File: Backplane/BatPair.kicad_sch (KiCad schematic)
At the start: 6 parts

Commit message: All parts are correct.
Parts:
- renumbered R31 to R22, R64 to R23, R65 to R24, R89 to R25, R90 to R26, R91 to R27
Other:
- removed sheet Current Control
- added sheet Current Control1 (Current Control.kicad_sch)

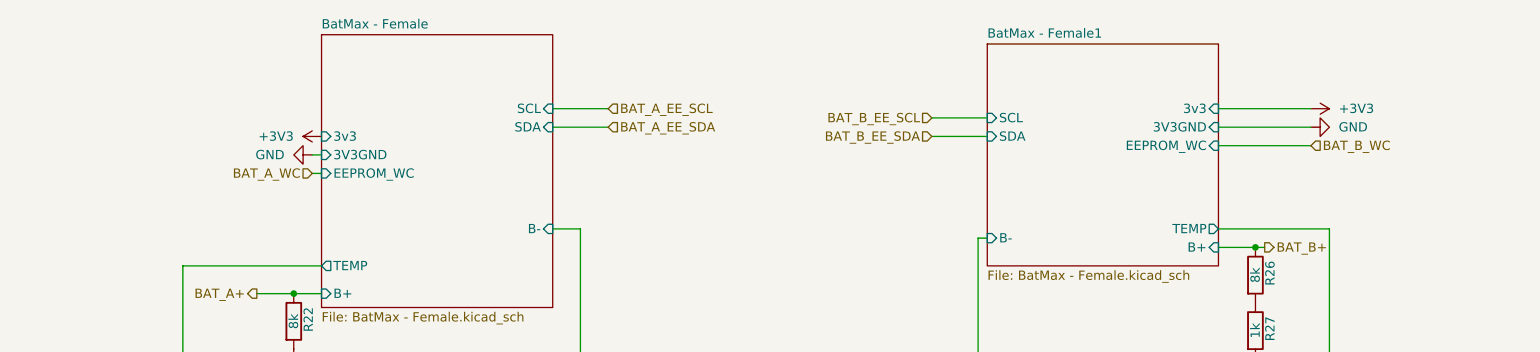
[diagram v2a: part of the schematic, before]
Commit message: First draft routing done.
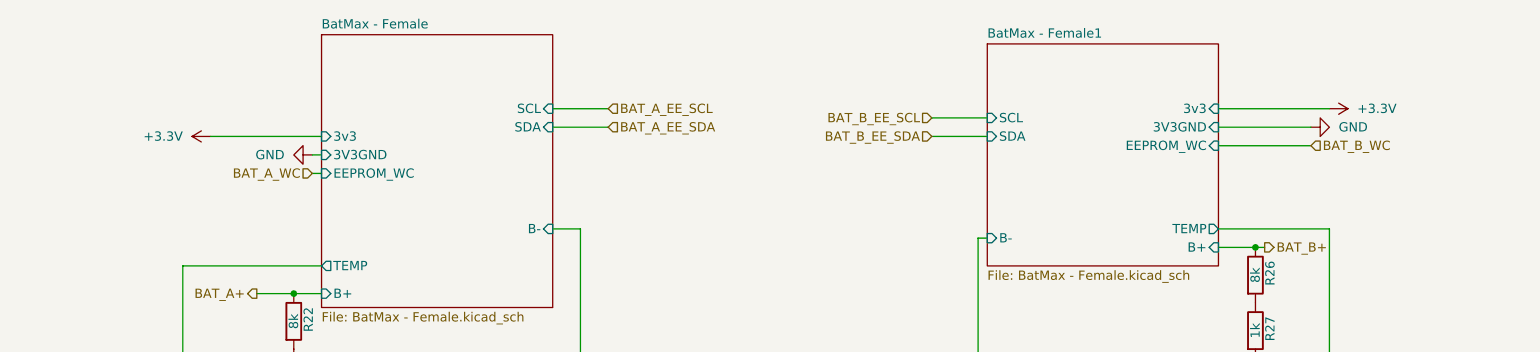
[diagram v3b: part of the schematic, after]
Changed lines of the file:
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@@
+	(wire
+		(pts
+			(xy 66.04 87.63) (xy 81.28 87.63)
+		)
+		(stroke
+			(width 0)
+			(type default)
+		)
+	)
 	(wire
 		(pts
@@
 	(wire
 		(pts
-			(xy 217.17 83.82) (xy 204.47 83.82)
-		)
-		(stroke
-			(width 0)
-			(type default)
-		)
-	)
-	(wire
-		(pts
 			(xy 237.49 129.54) (xy 237.49 130.81)
 		)
@@
 		(pts
 			(xy 73.66 140.97) (xy 59.69 140.97)
+		)
+		(stroke
+			(width 0)
+			(type default)
+		)
+	)
+	(wire
+		(pts
+			(xy 219.71 83.82) (xy 204.47 83.82)
 		)
 		(stroke
@@
 	)
 	(symbol
+		(lib_id "power:+3.3V")
+		(at 219.71 83.82 270)
+		(mirror x)
+		(unit 1)
+		(exclude_from_sim no)
+		(in_bom yes)
+		(on_board yes)
+		(dnp no)
+		(fields_autoplaced yes)
+		(property "Reference" "#PWR075"
+			(at 215.9 83.82 0)
+			(effects
+				(font
+					(size 1.27 1.27)
+				)
+				(hide yes)
+			)
+		)
+		(property "Value" "+3.3V"
+			(at 223.52 83.8199 90)
+			(effects
+				(font
+					(size 1.27 1.27)
+				)
+				(justify left)
+			)
+		)
+		(property "Footprint" ""
+			(at 219.71 83.82 0)
+			(effects
+				(font
+					(size 1.27 1.27)
+				)
+				(hide yes)
+			)
+		)
+		(property "Datasheet" ""
+			(at 219.71 83.82 0)
+			(effects
+				(font
+					(size 1.27 1.27)
+				)
+				(hide yes)
+			)
+		)
+		(property "Description" "Power symbol creates a global label with name \"+3.3V\""
+			(at 219.71 83.82 0)
+			(effects
+				(font
+					(size 1.27 1.27)
+				)
+				(hide yes)
+			)
+		)
+		(pin "1"
+		)
+		(instances
+			(project "Backplane"
+				(path "/4763d09e-4fb7-455a-b785-38411d748b6f/73c31c82-b4ce-4db9-85ed-23bc4db11f2f"
+					(reference "#PWR075")
+					(unit 1)
+				)
+				(path "/4763d09e-4fb7-455a-b785-38411d748b6f/af45f37b-7841-4d0a-9a92-a045ec353c82"
+					(reference "#PWR076")
+					(unit 1)
+				)
+			)
+		)
+	)
+	(symbol
+		(lib_id "power:+3.3V")
+		(at 66.04 87.63 90)
+		(unit 1)
+		(exclude_from_sim no)
+		(in_bom yes)
+		(on_board yes)
+		(dnp no)
+		(fields_autoplaced yes)
+		(property "Reference" "#PWR058"
+			(at 69.85 87.63 0)
+			(effects
+				(font
+					(size 1.27 1.27)
+				)
+				(hide yes)
+			)
+		)
+		(property "Value" "+3.3V"
+			(at 62.23 87.6299 90)
+			(effects
+				(font
+					(size 1.27 1.27)
+				)
+				(justify left)
+			)
+		)
+		(property "Footprint" ""
+			(at 66.04 87.63 0)
+			(effects
+				(font
+					(size 1.27 1.27)
+				)
+				(hide yes)
+			)
+		)
+		(property "Datasheet" ""
+			(at 66.04 87.63 0)
+			(effects
+				(font
+					(size 1.27 1.27)
+				)
+				(hide yes)
+			)
+		)
+		(property "Description" "Power symbol creates a global label with name \"+3.3V\""
+			(at 66.04 87.63 0)
+			(effects
+				(font
+					(size 1.27 1.27)
+				)
+				(hide yes)
+			)
+		)
+		(pin "1"
+		)
+		(instances
+			(project ""
+				(path "/4763d09e-4fb7-455a-b785-38411d748b6f/73c31c82-b4ce-4db9-85ed-23bc4db11f2f"
+					(reference "#PWR058")
+					(unit 1)
+				)
+				(path "/4763d09e-4fb7-455a-b785-38411d748b6f/af45f37b-7841-4d0a-9a92-a045ec353c82"
+					(reference "#PWR068")
+					(unit 1)
+				)
+			)
+		)
+	)
+	(symbol
 		(lib_id "power:GND")
 		(at 85.09 127 90)
@@
 					(unit 1)
 				)
-			)
-		)
-	)
-	(symbol
-		(lib_id "power:+3V3")
-		(at 217.17 83.82 270)
-		(unit 1)
-		(exclude_from_sim no)
-		(in_bom yes)
-		(on_board yes)
-		(dnp no)
-		(fields_autoplaced yes)
-		(property "Reference" "#PWR061"
-			(at 213.36 83.82 0)
-			(effects
-				(font
-					(size 1.27 1.27)
-				)
-				(hide yes)
-			)
-		)
-		(property "Value" "+3V3"
-			(at 220.98 83.8199 90)
-			(effects
-				(font
-					(size 1.27 1.27)
-				)
-				(justify left)
-			)
-		)
-		(property "Footprint" ""
-			(at 217.17 83.82 0)
-			(effects
-				(font
-					(size 1.27 1.27)
-				)
-				(hide yes)
-			)
-		)
-		(property "Datasheet" ""
-			(at 217.17 83.82 0)
-			(effects
-				(font
-					(size 1.27 1.27)
-				)
-				(hide yes)
-			)
-		)
-		(property "Description" "Power symbol creates a global label with name \"+3V3\""
-			(at 217.17 83.82 0)
-			(effects
-				(font
-					(size 1.27 1.27)
-				)
-				(hide yes)
-			)
-		)
-		(pin "1"
-		)
-		(instances
-			(project "Backplane"
-				(path "/4763d09e-4fb7-455a-b785-38411d748b6f/73c31c82-b4ce-4db9-85ed-23bc4db11f2f"
-					(reference "#PWR061")
-					(unit 1)
-				)
-				(path "/4763d09e-4fb7-455a-b785-38411d748b6f/af45f37b-7841-4d0a-9a92-a045ec353c82"
-					(reference "#PWR071")
-					(unit 1)
-				)
-			)
-		)
-	)
-	(symbol
-		(lib_id "power:+3V3")
-		(at 81.28 87.63 90)
-		(mirror x)
-		(unit 1)
-		(exclude_from_sim no)
-		(in_bom yes)
-		(on_board yes)
-		(dnp no)
-		(fields_autoplaced yes)
-		(property "Reference" "#PWR058"
-			(at 85.09 87.63 0)
-			(effects
-				(font
-					(size 1.27 1.27)
-				)
-				(hide yes)
-			)
-		)
-		(property "Value" "+3V3"
-			(at 77.47 87.6299 90)
-			(effects
-				(font
-					(size 1.27 1.27)
-				)
-				(justify left)
-			)
-		)
-		(property "Footprint" ""
-			(at 81.28 87.63 0)
-			(effects
-				(font
-					(size 1.27 1.27)
-				)
-				(hide yes)
-			)
-		)
-		(property "Datasheet" ""
-			(at 81.28 87.63 0)
-			(effects
-				(font
-					(size 1.27 1.27)
-				)
-				(hide yes)
-			)
-		)
-		(property "Description" "Power symbol creates a global label with name \"+3V3\""
-			(at 81.28 87.63 0)
-			(effects
-				(font
-					(size 1.27 1.27)
-				)
-				(hide yes)
-			)
-		)
-		(pin "1"
-		)
-		(instances
-			(project "Backplane"
-				(path "/4763d09e-4fb7-455a-b785-38411d748b6f/73c31c82-b4ce-4db9-85ed-23bc4db11f2f"
-					(reference "#PWR058")
-					(unit 1)
-				)
-				(path "/4763d09e-4fb7-455a-b785-38411d748b6f/af45f37b-7841-4d0a-9a92-a045ec353c82"
-					(reference "#PWR068")
-					(unit 1)
-				)

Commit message: added
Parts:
- removed R22, R26: 8k, Resistor_SMD:R_1206_3216Metric_Pad1.30x1.75mm_HandSolder, symbol Device:R
- removed R23, R24, R25, R27: 1k, Resistor_SMD:R_1206_3216Metric_Pad1.30x1.75mm_HandSolder, symbol Device:R
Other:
- removed sheet ADS1118
- removed sheet ADS1119
- removed sheet Current Control1
